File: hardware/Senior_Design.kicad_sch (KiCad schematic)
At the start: 0 parts

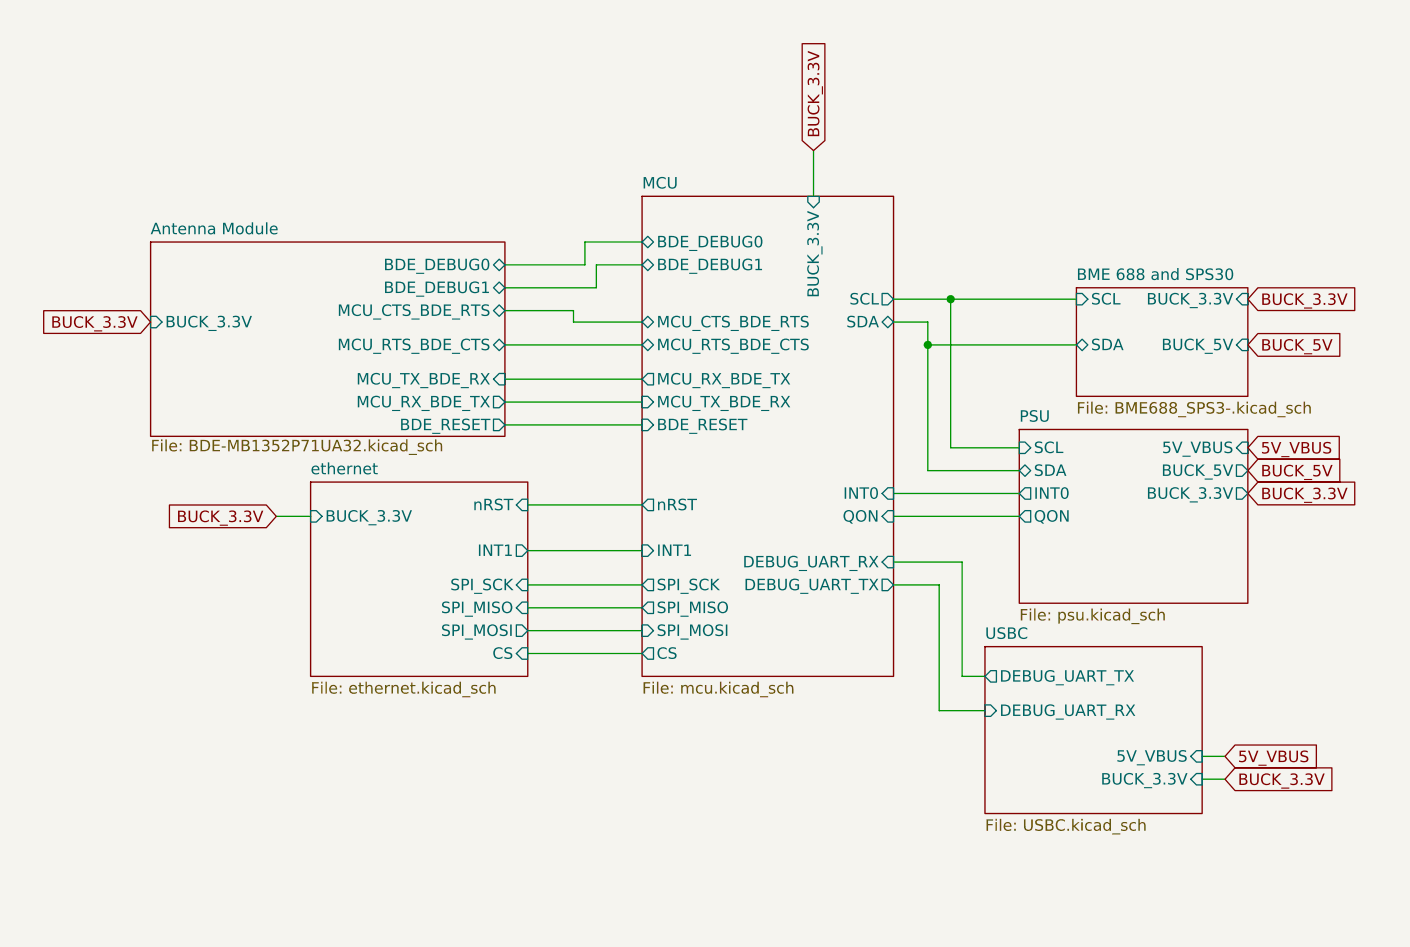
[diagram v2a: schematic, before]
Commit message: Fixed MCU JTAG/Reordered pages
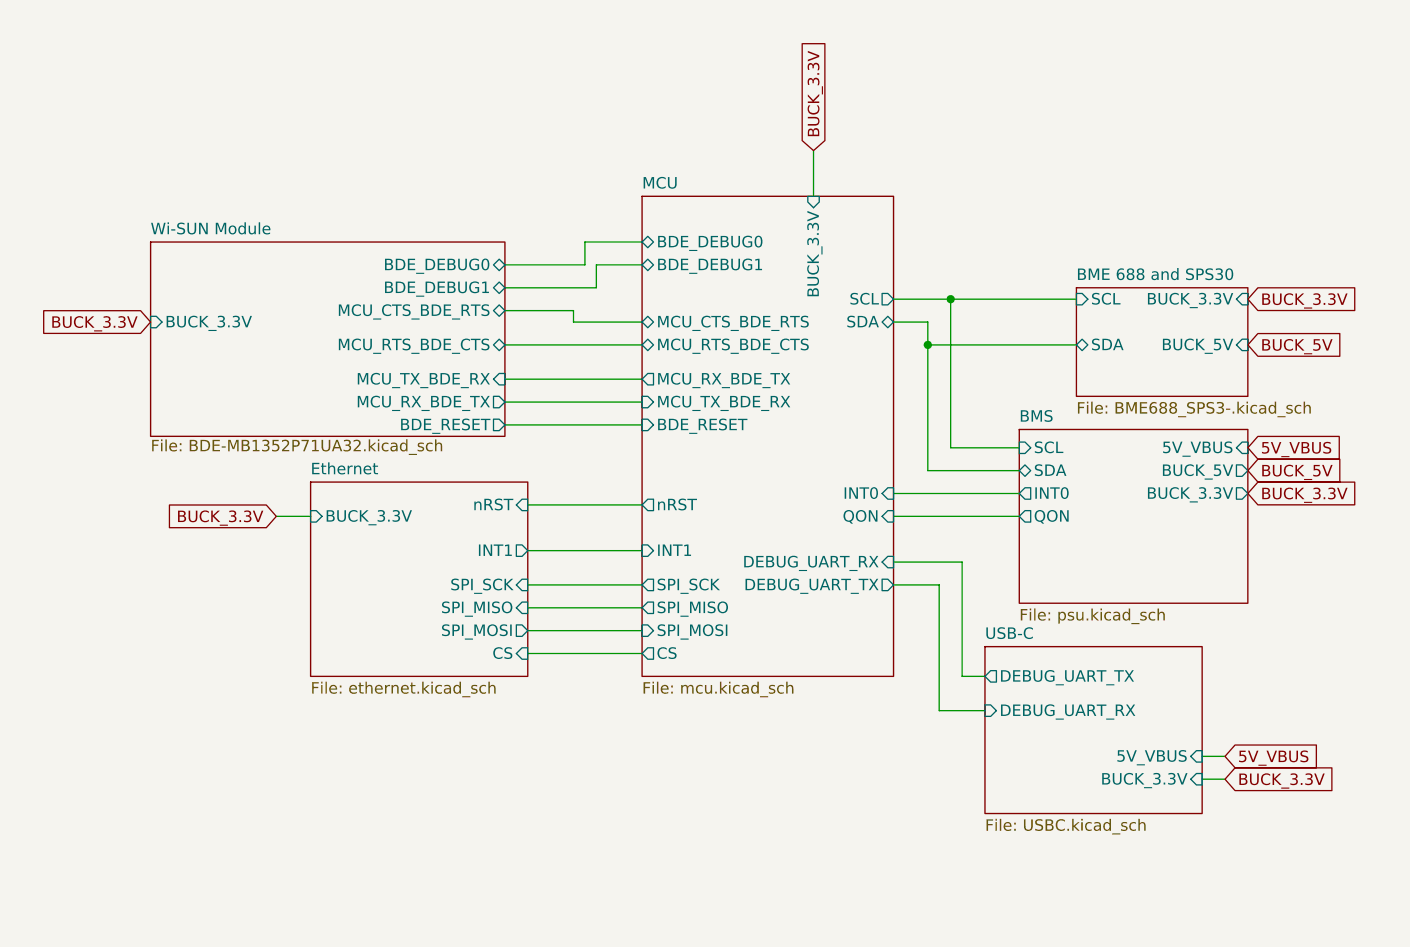
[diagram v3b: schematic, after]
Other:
- sheet Antenna Module renamed Wi-SUN Module
- sheet PSU renamed BMS
- sheet USBC renamed USB-C
- sheet ethernet renamed Ethernet
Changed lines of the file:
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@@
 			(color 0 0 0 0.0000)
 		)
-		(property "Sheetname" "PSU"
+		(property "Sheetname" "BMS"
 			(at 172.72 82.3464 0)
 			(effects
@@
 			(project "Senior_Design"
 				(path "/8f5928e8-0fc1-4443-a20f-3bfeb956761e"
-					(page "2")
+					(page "3")
 				)
 			)
@@
 			(project "Senior_Design"
 				(path "/8f5928e8-0fc1-4443-a20f-3bfeb956761e"
-					(page "4")
+					(page "5")
 				)
 			)
@@
 			(color 0 0 0 0.0000)
 		)
-		(property "Sheetname" "USBC"
+		(property "Sheetname" "USB-C"
 			(at 168.91 106.4764 0)
 			(effects
@@
 			(project "Senior_Design"
 				(path "/8f5928e8-0fc1-4443-a20f-3bfeb956761e"
-					(page "7")
+					(page "6")
 				)
 			)
@@
 			(color 0 0 0 0.0000)
 		)
-		(property "Sheetname" "ethernet"
+		(property "Sheetname" "Ethernet"
 			(at 93.98 88.1884 0)
 			(effects
@@
 			(project "Senior_Design"
 				(path "/8f5928e8-0fc1-4443-a20f-3bfeb956761e"
-					(page "3")
+					(page "7")
 				)
 			)
@@
 			(color 0 0 0 0.0000)
 		)
-		(property "Sheetname" "Antenna Module"
+		(property "Sheetname" "Wi-SUN Module"
 			(at 76.2 61.5184 0)
 			(effects
@@
 			(project "Senior_Design"
 				(path "/8f5928e8-0fc1-4443-a20f-3bfeb956761e"
-					(page "5")
+					(page "4")
 				)
 			)
@@
 			(project "Senior_Design"
 				(path "/8f5928e8-0fc1-4443-a20f-3bfeb956761e"
-					(page "6")
-				)
-			)
+					(page "2")
+				)
+			)

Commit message: Replaced 3.3V symbol
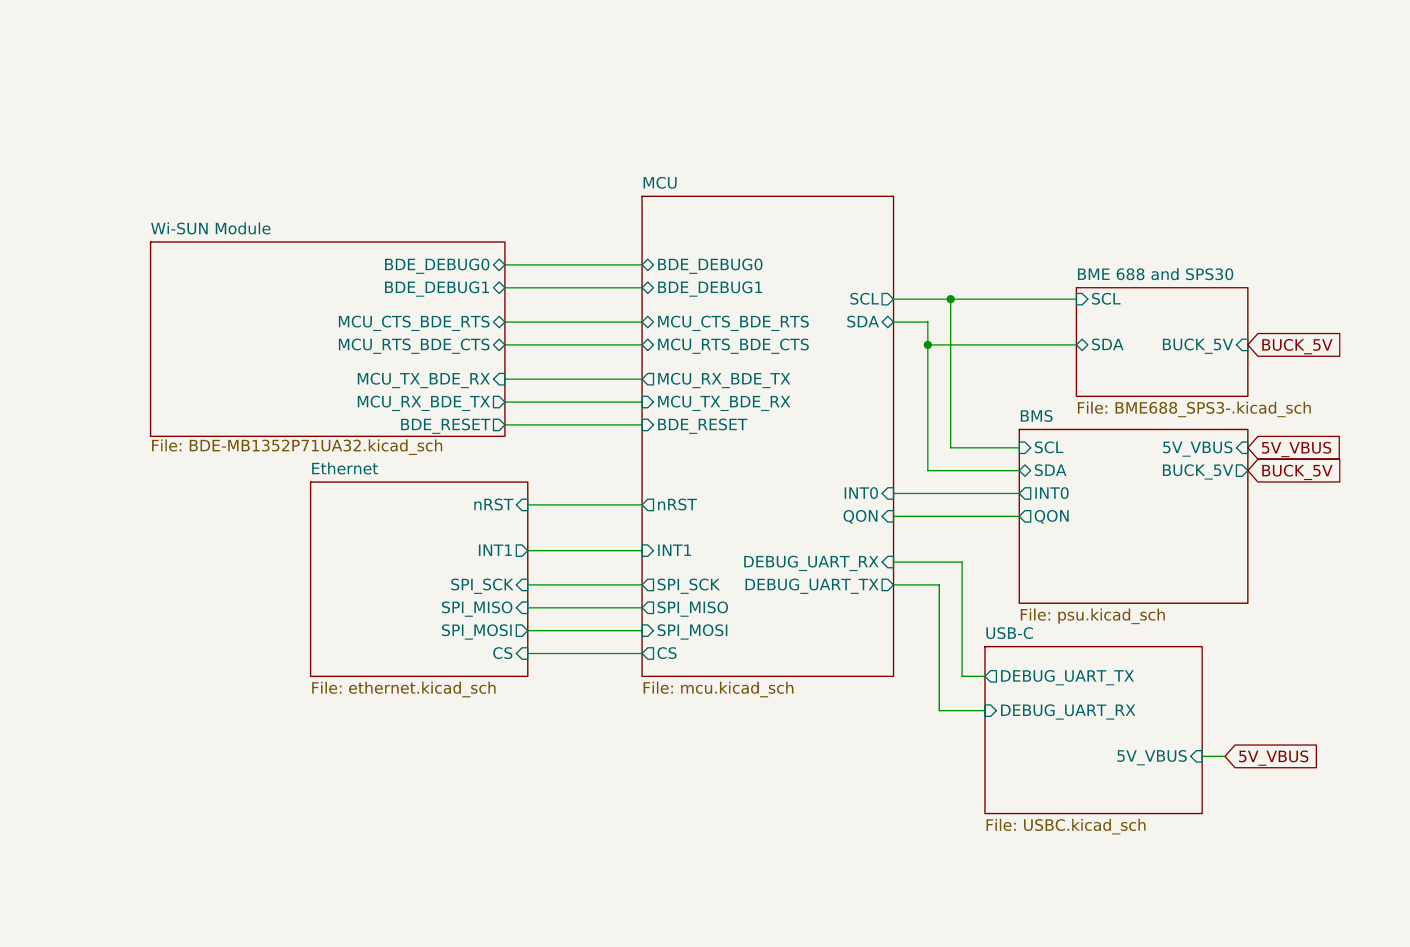
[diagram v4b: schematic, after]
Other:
- sheet BME 688 and SPS30 ports: added none; removed BUCK_3.3V
- sheet BMS ports: added none; removed BUCK_3.3V
- sheet Ethernet ports: added none; removed BUCK_3.3V
- sheet MCU ports: added none; removed BUCK_3.3V
- sheet USB-C ports: added none; removed BUCK_3.3V
- sheet Wi-SUN Module ports: added none; removed BUCK_3.3V

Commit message: updated major symbol and footprints
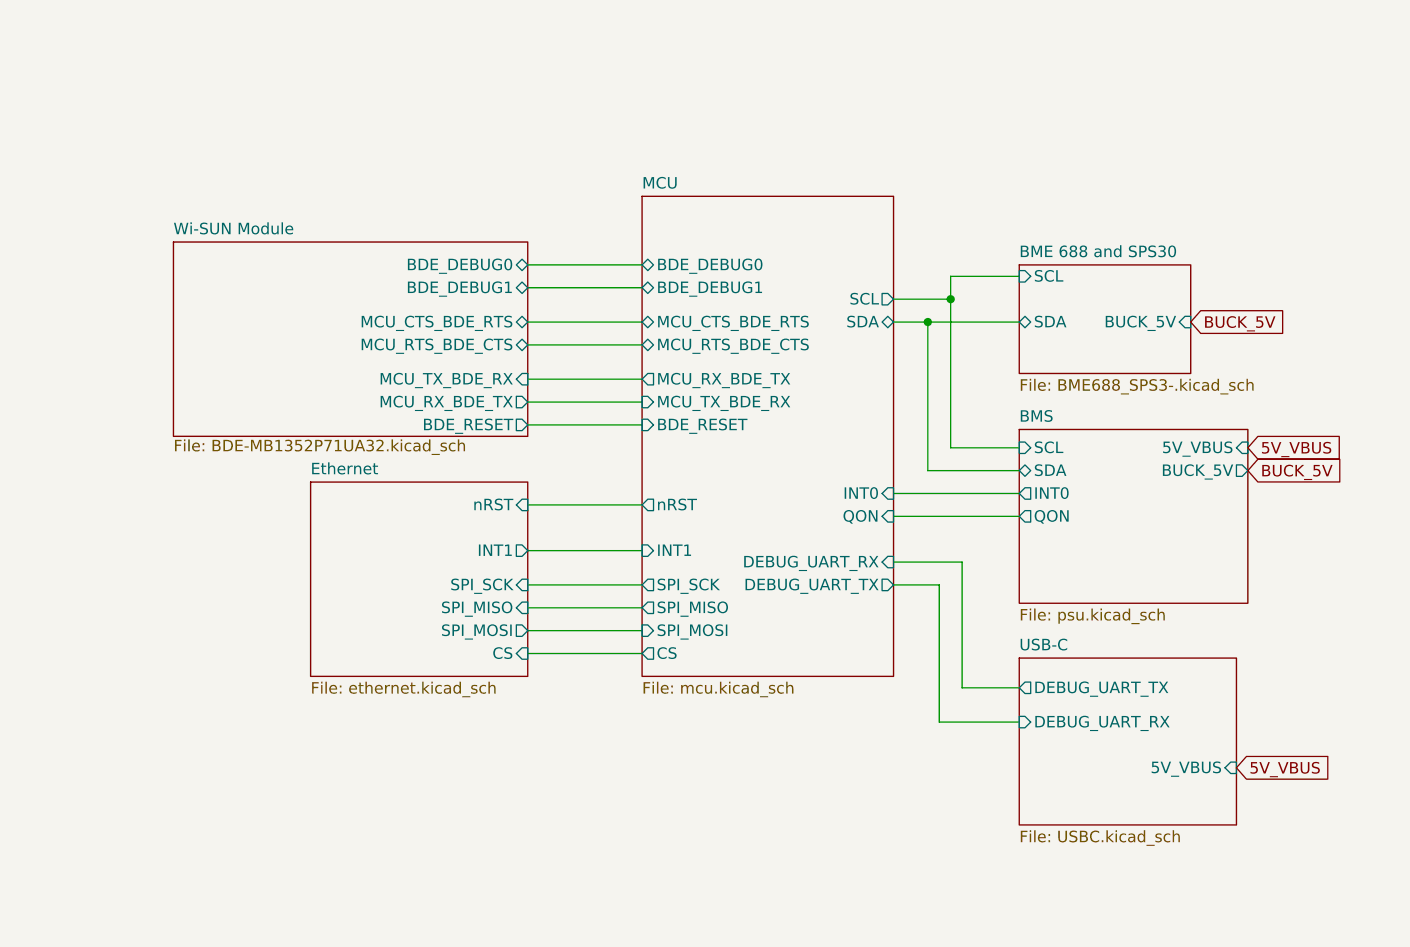
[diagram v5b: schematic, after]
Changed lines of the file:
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@@
 	)
 	(junction
-		(at 162.56 73.66)
+		(at 162.56 71.12)
 		(diameter 0)
 		(color 0 0 0 0)
@@
 	(wire
 		(pts
-			(xy 115.57 77.47) (xy 130.81 77.47)
+			(xy 118.11 77.47) (xy 130.81 77.47)
 		)
 		(stroke
@@
 	(wire
 		(pts
-			(xy 166.37 110.49) (xy 168.91 110.49)
+			(xy 166.37 111.76) (xy 172.72 111.76)
 		)
 		(stroke
@@
 	(wire
 		(pts
-			(xy 162.56 73.66) (xy 179.07 73.66)
+			(xy 162.56 71.12) (xy 172.72 71.12)
+		)
+		(stroke
+			(width 0)
+			(type default)
+		)
+	)
+	(wire
+		(pts
+			(xy 165.1 66.04) (xy 165.1 68.58)
 		)
 		(stroke
@@
 	(wire
 		(pts
-			(xy 163.83 100.33) (xy 163.83 114.3)
-		)
-		(stroke
-			(width 0)
-			(type default)
-		)
-	)
-	(wire
-		(pts
-			(xy 115.57 67.31) (xy 130.81 67.31)
-		)
-		(stroke
-			(width 0)
-			(type default)
-		)
-	)
-	(wire
-		(pts
-			(xy 165.1 68.58) (xy 179.07 68.58)
-		)
-		(stroke
-			(width 0)
-			(type default)
-		)
-	)
-	(wire
-		(pts
-			(xy 115.57 73.66) (xy 130.81 73.66)
+			(xy 163.83 100.33) (xy 163.83 115.57)
+		)
+		(stroke
+			(width 0)
+			(type default)
+		)
+	)
+	(wire
+		(pts
+			(xy 118.11 67.31) (xy 130.81 67.31)
+		)
+		(stroke
+			(width 0)
+			(type default)
+		)
+	)
+	(wire
+		(pts
+			(xy 165.1 66.04) (xy 172.72 66.04)
+		)
+		(stroke
+			(width 0)
+			(type default)
+		)
+	)
+	(wire
+		(pts
+			(xy 118.11 73.66) (xy 130.81 73.66)
 		)
 		(stroke
@@
 	(wire
 		(pts
-			(xy 162.56 73.66) (xy 162.56 87.63)
-		)
-		(stroke
-			(width 0)
-			(type default)
-		)
-	)
-	(wire
-		(pts
-			(xy 166.37 97.79) (xy 166.37 110.49)
-		)
-		(stroke
-			(width 0)
-			(type default)
-		)
-	)
-	(wire
-		(pts
-			(xy 168.91 114.3) (xy 163.83 114.3)
+			(xy 166.37 97.79) (xy 166.37 111.76)
+		)
+		(stroke
+			(width 0)
+			(type default)
+		)
+	)
+	(wire
+		(pts
+			(xy 172.72 115.57) (xy 163.83 115.57)
 		)
 		(stroke
@@
 	(wire
 		(pts
-			(xy 115.57 71.12) (xy 130.81 71.12)
-		)
-		(stroke
-			(width 0)
-			(type default)
-		)
-	)
-	(wire
-		(pts
-			(xy 195.58 119.38) (xy 193.04 119.38)
+			(xy 118.11 71.12) (xy 130.81 71.12)
 		)
 		(stroke
@@
 	(wire
 		(pts
-			(xy 115.57 82.55) (xy 130.81 82.55)
-		)
-		(stroke
-			(width 0)
-			(type default)
-		)
-	)
-	(wire
-		(pts
-			(xy 115.57 80.01) (xy 130.81 80.01)
+			(xy 118.11 82.55) (xy 130.81 82.55)
+		)
+		(stroke
+			(width 0)
+			(type default)
+		)
+	)
+	(wire
+		(pts
+			(xy 118.11 80.01) (xy 130.81 80.01)
 		)
 		(stroke
@@
 	(wire
 		(pts
-			(xy 115.57 64.77) (xy 130.81 64.77)
-		)
-		(stroke
-			(width 0)
-			(type default)
-		)
-	)
-	(wire
-		(pts
-			(xy 162.56 71.12) (xy 162.56 73.66)
+			(xy 118.11 64.77) (xy 130.81 64.77)
+		)
+		(stroke
+			(width 0)
+			(type default)
+		)
+	)
+	(wire
+		(pts
+			(xy 162.56 71.12) (xy 162.56 87.63)
 		)
 		(stroke
@@
 	(global_label "BUCK_5V"
 		(shape input)
-		(at 198.12 73.66 0)
+		(at 191.77 71.12 0)
 		(fields_autoplaced yes)
 		(effects
@@
 		)
 		(property "Intersheetrefs" "${INTERSHEET_REFS}"
-			(at 209.5114 73.66 0)
+			(at 203.1614 71.12 0)
 			(effects
 				(font
@@
 	(global_label "5V_VBUS"
 		(shape input)
-		(at 195.58 119.38 0)
+		(at 196.85 120.65 0)
 		(fields_autoplaced yes)
 		(effects
@@
 		)
 		(property "Intersheetrefs" "${INTERSHEET_REFS}"
-			(at 206.7295 119.38 0)
+			(at 207.9995 120.65 0)
 			(effects
 				(font
@@
 	)
 	(sheet
-		(at 179.07 67.31)
+		(at 172.72 64.77)
 		(size 19.05 12.065)
 		(exclude_from_sim no)
@@
 		)
 		(property "Sheetname" "BME 688 and SPS30"
-			(at 179.07 66.5984 0)
+			(at 172.72 64.0584 0)
 			(effects
 				(font
@@
 		)
 		(property "Sheetfile" "BME688_SPS3-.kicad_sch"
-			(at 179.07 79.9596 0)
+			(at 172.72 77.4196 0)
 			(effects
 				(font
@@
 		)
 		(pin "BUCK_5V" input
-			(at 198.12 73.66 0)
+			(at 191.77 71.12 0)
 			(effects
 				(font
@@
 		)
 		(pin "SCL" input
-			(at 179.07 68.58 180)
+			(at 172.72 66.04 180)
 			(effects
 				(font
@@
 		)
 		(pin "SDA" bidirectional
-			(at 179.07 73.66 180)
+			(at 172.72 71.12 180)
 			(effects
 				(font
@@
 	)
 	(sheet
-		(at 168.91 107.188)
+		(at 172.72 108.458)
 		(size 24.13 18.542)
 		(exclude_from_sim no)
@@
 		)
 		(property "Sheetname" "USB-C"
-			(at 168.91 106.4764 0)
+			(at 172.72 107.7464 0)
 			(effects
 				(font
@@
 		)
 		(property "Sheetfile" "USBC.kicad_sch"
-			(at 168.91 126.3146 0)
+			(at 172.72 127.5846 0)
 			(effects
 				(font
@@
 		)
 		(pin "DEBUG_UART_RX" input
-			(at 168.91 114.3 180)
+			(at 172.72 115.57 180)
 			(effects
 				(font
@@
 		)
 		(pin "DEBUG_UART_TX" output
-			(at 168.91 110.49 180)
+			(at 172.72 111.76 180)
 			(effects
 				(font
@@
 		)
 		(pin "5V_VBUS" input
-			(at 193.04 119.38 0)
+			(at 196.85 120.65 0)
 			(effects
 				(font
@@
 	)
 	(sheet
-		(at 76.2 62.23)
+		(at 78.74 62.23)
 		(size 39.37 21.59)
 		(exclude_from_sim no)
@@
 		)
 		(property "Sheetname" "Wi-SUN Module"
-			(at 76.2 61.5184 0)
+			(at 78.74 61.5184 0)
 			(effects
 				(font
@@
 		)
 		(property "Sheetfile" "BDE-MB1352P71UA32.kicad_sch"
-			(at 76.2 84.1506 0)
+			(at 78.74 84.1506 0)
 			(effects
 				(font
@@
 		)
 		(pin "MCU_CTS_BDE_RTS" bidirectional
-			(at 115.57 71.12 0)
+			(at 118.11 71.12 0)
 			(effects
 				(font
@@
 		)
 		(pin "MCU_RTS_BDE_CTS" bidirectional
-			(at 115.57 73.66 0)
+			(at 118.11 73.66 0)
 			(effects
 				(font
@@
 		)
 		(pin "BDE_DEBUG0" bidirectional
-			(at 115.57 64.77 0)
+			(at 118.11 64.77 0)
 			(effects
 				(font
@@
 		)
 		(pin "MCU_RX_BDE_TX" output
-			(at 115.57 80.01 0)
+			(at 118.11 80.01 0)
 			(effects
 				(font
@@
 		)
 		(pin "MCU_TX_BDE_RX" input
-			(at 115.57 77.47 0)
+			(at 118.11 77.47 0)
 			(effects
 				(font
@@
 		)
 		(pin "BDE_DEBUG1" bidirectional
-			(at 115.57 67.31 0)
+			(at 118.11 67.31 0)
 			(effects
 				(font
@@
 		)
 		(pin "BDE_RESET" output
-			(at 115.57 82.55 0)
-			(effects
-				(font
+			(at 118.11 82.55 0)
+			(effects
+				(font

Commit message: updated 5V power and pin
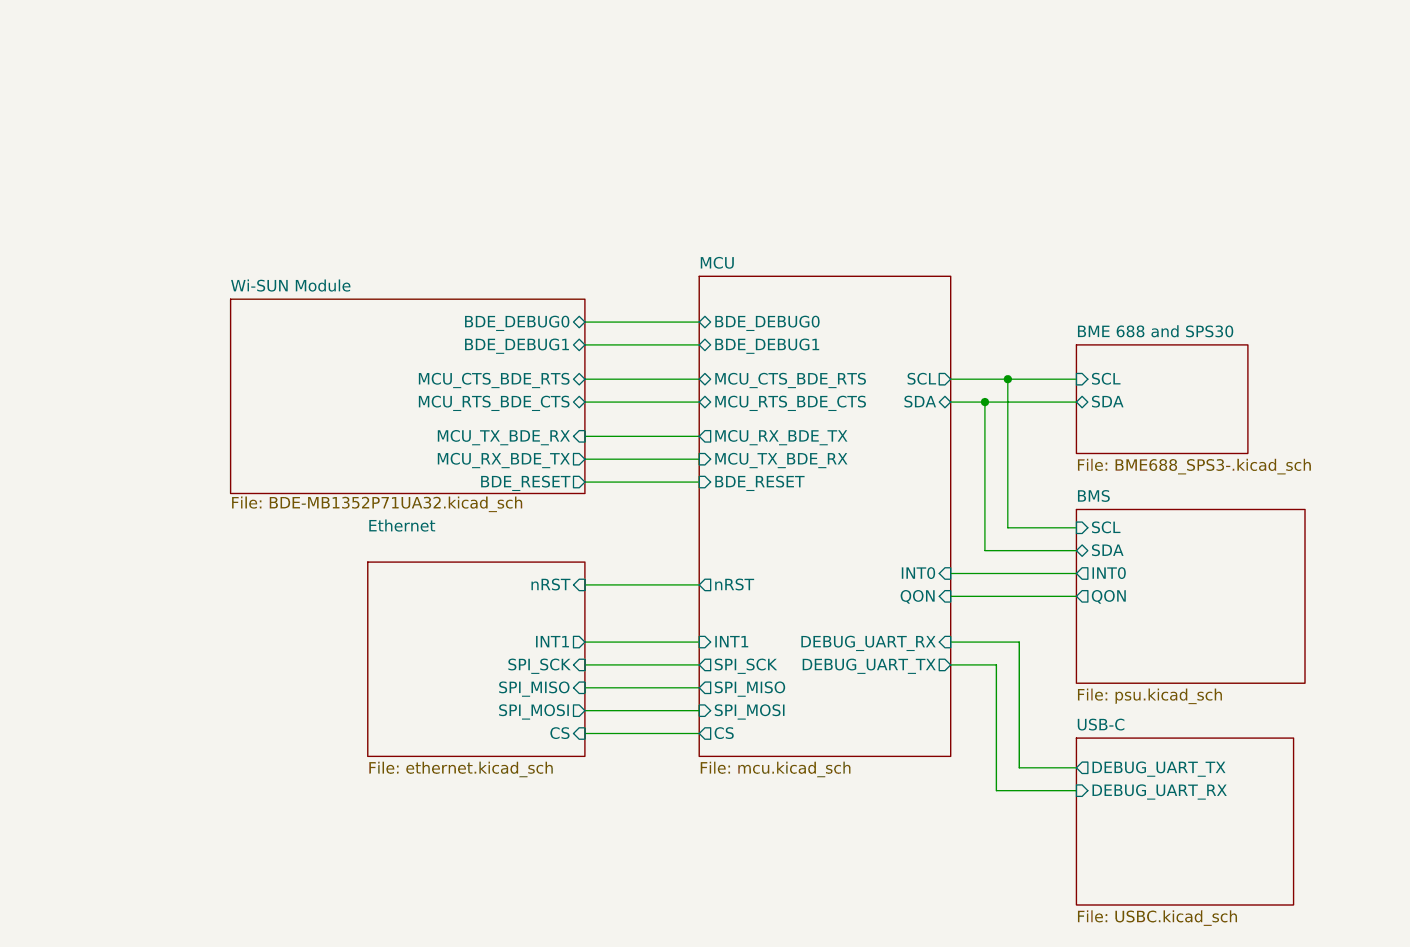
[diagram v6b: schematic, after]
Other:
- sheet BME 688 and SPS30 ports: added none; removed BUCK_5V
- sheet BMS ports: added none; removed 5V_VBUS, BUCK_5V
- sheet USB-C ports: added none; removed 5V_VBUS
